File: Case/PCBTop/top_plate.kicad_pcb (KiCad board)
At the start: 2 copper layers, 143.5 x 115.5 mm, 5 parts

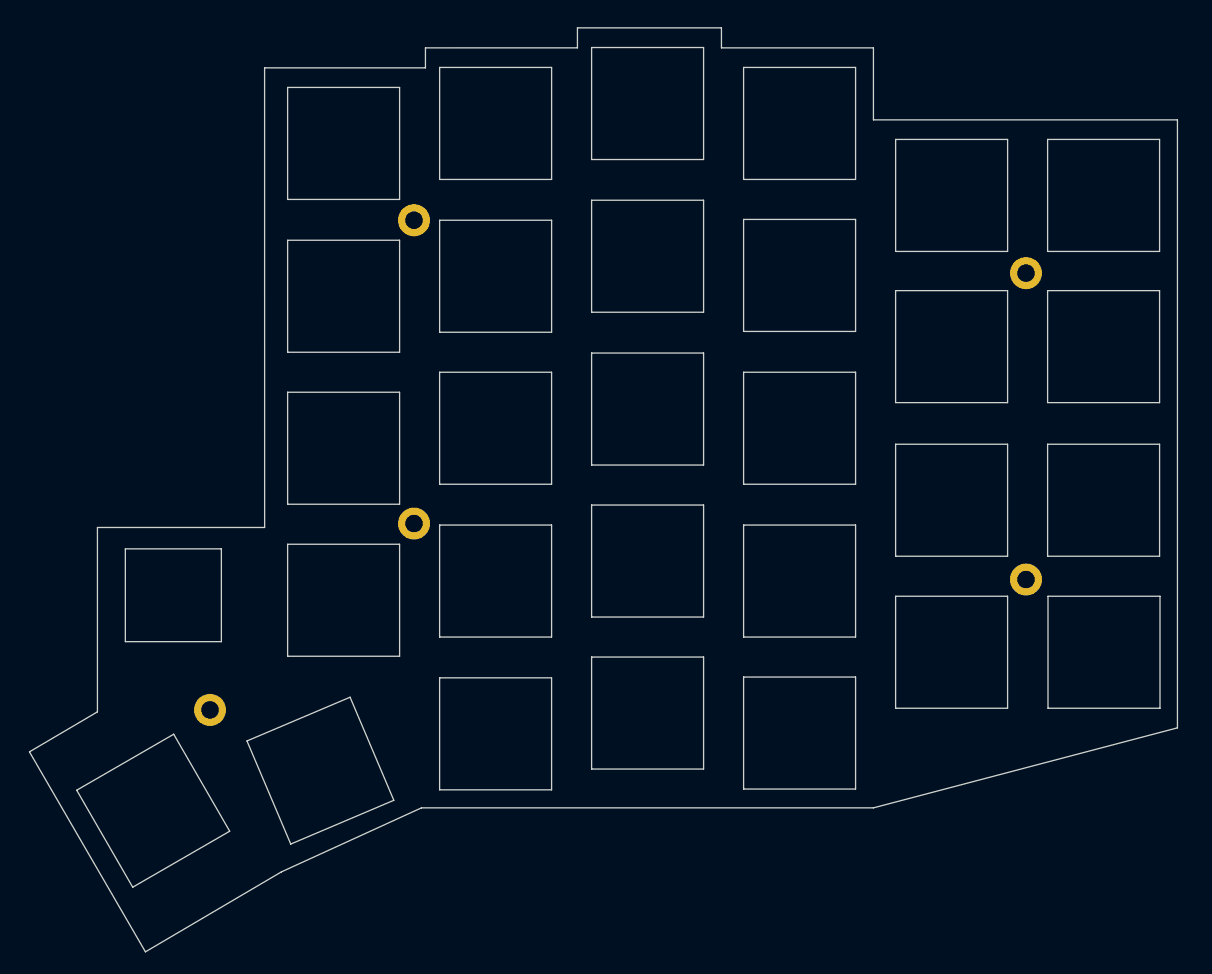
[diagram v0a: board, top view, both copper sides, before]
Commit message: Add logos and credits on all boards
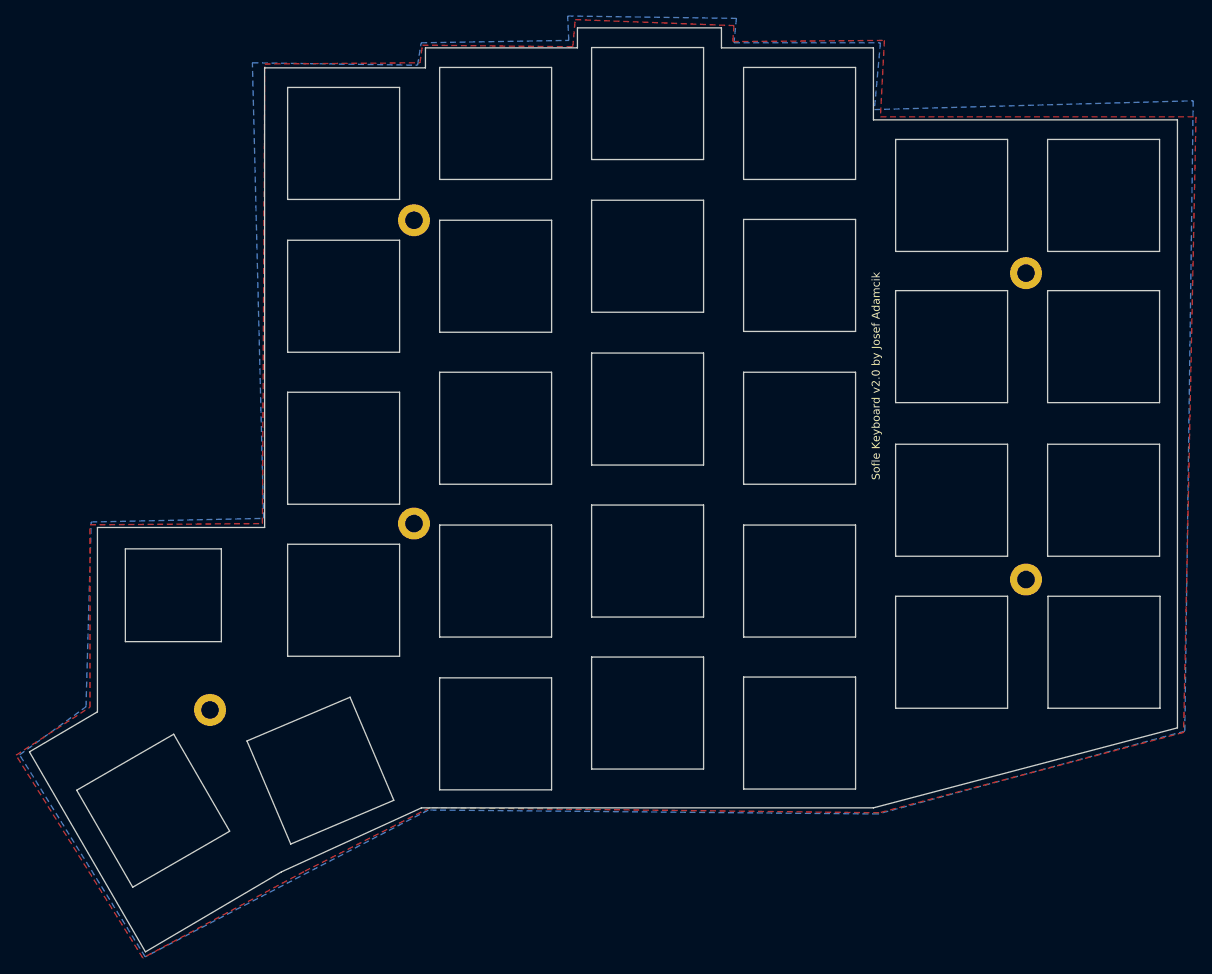
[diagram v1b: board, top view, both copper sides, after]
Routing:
- added copper zone on B.Cu, net (none)
- added copper zone on F.Cu, net (none)
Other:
- board text added: "Sofle Keyboard v2.0 by Josef Adamcik"
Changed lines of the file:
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@@
   (general
     (thickness 1.6)
-    (drawings 139)
+    (drawings 141)
     (tracks 0)
     (zones 0)
@@
     )
     (pad 5 thru_hole circle (at 0 0) (size 4 4) (drill 2.2) (layers *.Cu *.Mask))
+  )
+  (gr_text "Sofle Keyboard v2.0  by Josef Adamcik" (at 130 69.8 90) (layer B.SilkS)
+    (effects (font (size 1 1) (thickness 0.15)) (justify mirror))
+  )
+  (gr_text "Sofle Keyboard v2.0 by Josef Adamcik" (at 130 69.65 90) (layer F.SilkS)
+    (effects (font (size 1 1) (thickness 0.15)))
   )
   (gr_line (start 53.574549 31.133314) (end 73.680951 31.131114) (layer Edge.Cuts) (width 0.1))
@@
   (gr_line (start 69.728727 122.68758) (end 56.843357 128.15872) (layer Edge.Cuts) (width 0.1))
   (gr_line (start 56.843357 128.15872) (end 51.372219 115.270805) (layer Edge.Cuts) (width 0.1))
+  (zone (net 0) (net_name "") (layer F.Cu) (hatch edge 0.508)
+    (connect_pads (clearance 0.508))
+    (min_thickness 0.254)
+    (fill yes (arc_segments 32) (thermal_gap 0.508) (thermal_bridge_width 0.508))
+    (polygon
+      (pts
+        (xy 112.25 25.85) (xy 112.1 27.85) (xy 131.05 27.7) (xy 130.55 37.25) (xy 170 37.25)
+        (xy 168.45 114.2) (xy 130.4 124.25) (xy 74.25 123.6) (xy 58.5 131.6) (xy 38.35 142.4)
+        (xy 22.5 117.05) (xy 31.75 111.05) (xy 31.75 88.25) (xy 53.3 88.1) (xy 53.6 30.65)
+        (xy 73 30.5) (xy 73.3 28.3) (xy 92.1 28.5) (xy 92.4 25.1)
+      )
+    )
+  )
+  (zone (net 0) (net_name "") (layer B.Cu) (hatch edge 0.508)
+    (connect_pads (clearance 0.508))
+    (min_thickness 0.254)
+    (fill yes (arc_segments 32) (thermal_gap 0.508) (thermal_bridge_width 0.508))
+    (polygon
+      (pts
+        (xy 112.55 24.95) (xy 112.25 28) (xy 130.55 28) (xy 129.8 36.35) (xy 169.65 35.25)
+        (xy 168.6 114.05) (xy 130.25 124.4) (xy 74.05 123.9) (xy 38.65 142.25) (xy 22.95 117)
+        (xy 31.25 111) (xy 31.9 87.9) (xy 53.45 87.45) (xy 52.05 30.5) (xy 72.7 30.8)
+        (xy 73.15 28) (xy 91.6 27.7) (xy 91.45 24.65)
+      )
+    )
+  )
 )
